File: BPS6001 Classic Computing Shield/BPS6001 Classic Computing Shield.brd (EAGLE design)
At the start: 119.4 x 58.7 mm, 85 parts, among them IC1 MAX3232CSE, X1 VGA

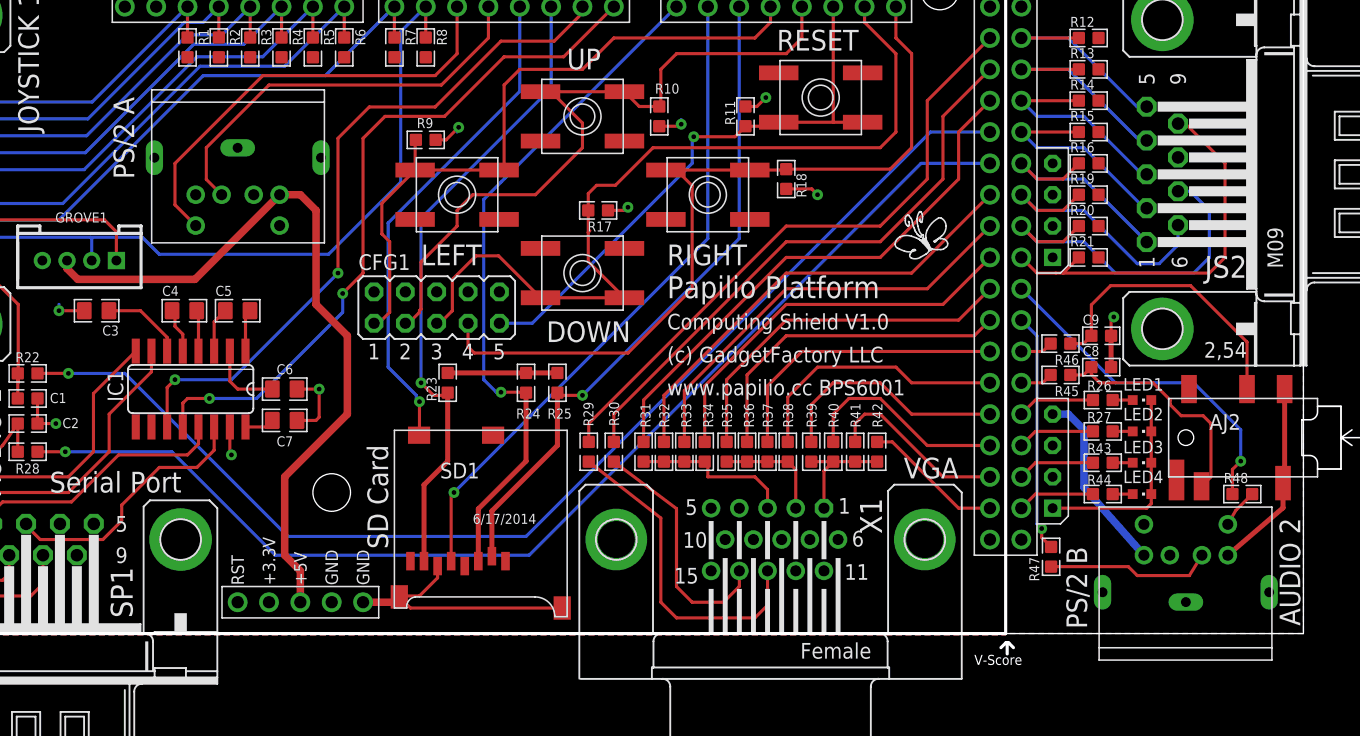
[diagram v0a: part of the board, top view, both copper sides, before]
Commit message: Fix the PS/2 connectors.
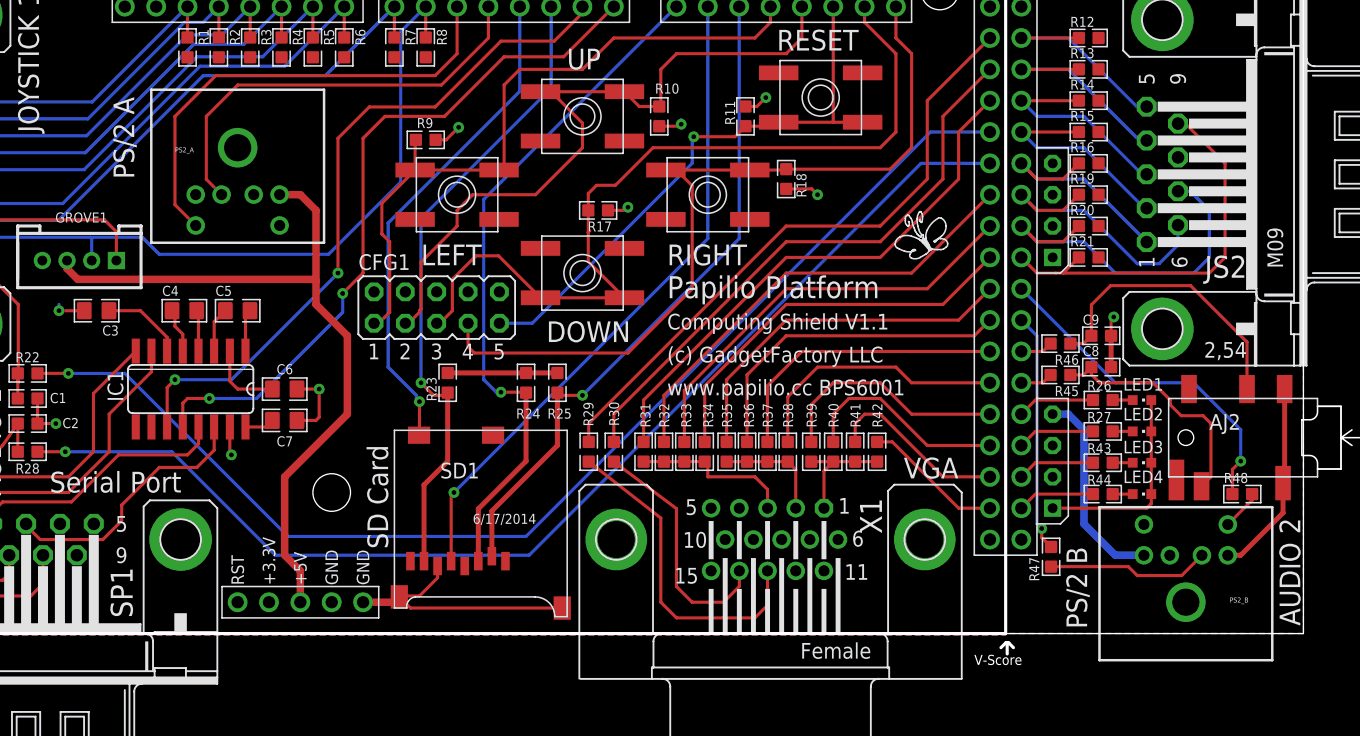
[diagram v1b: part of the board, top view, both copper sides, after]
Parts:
- PS2_A, PS2_B: value CON_PS/2 -> MINI-DIN6PTH; device usb1:PS/2 -> SparkFun-Connectors:MINI-DIN6
- moved PS2_A 8.51 mm to (33.0, 44.1)
- moved PS2_B 8.51 mm to (109.9, -2.16)
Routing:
- net PS2CLK1: track 36.1 -> 38.3 mm
- net 5V0_PS2: track 15.1 -> 16.6 mm
- net PS2DAT1: track 33.4 -> 34.9 mm
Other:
- board text added: "Computing Shield V1.1"
- board text removed: "Computing Shield V1.0"
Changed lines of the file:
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@@
 <setting verticaltext="up"/>
 </settings>
-<grid distance="0.05" unitdist="inch" unit="mm" style="lines" multiple="1" display="yes" altdistance="0.005" altunitdist="inch" altunit="inch"/>
+<grid distance="0.05" unitdist="inch" unit="inch" style="lines" multiple="1" display="yes" altdistance="0.005" altunitdist="inch" altunit="inch"/>
 <layers>
 <layer number="1" name="Top" color="4" fill="1" visible="yes" active="yes"/>
@@
 <wire x1="0" y1="0" x2="0" y2="55.88" width="0.254" layer="20"/>
 <text x="67.818" y="27.178" size="1.778" layer="21" ratio="12">Papilio Platform</text>
-<text x="67.818" y="24.638" size="1.27" layer="21" ratio="10">Computing Shield V1.0</text>
+<text x="67.818" y="24.638" size="1.27" layer="21" ratio="10">Computing Shield V1.1</text>
 <text x="24.638" y="36.83" size="1.6764" layer="21" ratio="15" rot="R90">PS/2 A</text>
 <text x="103.759" y="53.34" size="1.6764" layer="21" ratio="15">Joystick 2</text>
@@
 <attribute name="BOM" value="EXCLUDE" x="88.519" y="31.75" size="1.778" layer="27" display="off"/>
 </element>
-<element name="PS2_B" library="usb1" package="PS/2" value="CON_PS/2" x="109.855" y="6.35" rot="R180">
-<attribute name="PARTNO" value="MD-60S" x="109.855" y="6.35" size="1.778" layer="27" rot="R180" display="off"/>
-</element>
-<element name="PS2_A" library="usb1" package="PS/2" value="CON_PS/2" x="33.02" y="35.56">
-<attribute name="PARTNO" value="MD-60S" x="33.02" y="35.56" size="1.778" layer="27" display="off"/>
-</element>
 <element name="R9" library="GadgetFactory" package="0603" value="47K" x="48.26" y="40.005" smashed="yes" rot="R180">
 <attribute name="NAME" x="48.871" y="41.772" size="0.8128" layer="25" font="vector" ratio="16" rot="R180"/>
@@
 <attribute name="PARTNO" value="M20-9720545" x="49.149" y="26.416" size="1.778" layer="27" display="off"/>
 </element>
+<element name="PS2_B" library="SparkFun-Connectors" package="MINI-DIN6" value="MINI-DIN6PTH" x="109.855" y="-2.159" rot="R180"/>
+<element name="PS2_A" library="SparkFun-Connectors" package="MINI-DIN6" value="MINI-DIN6PTH" x="33.02" y="44.069"/>
 </elements>
 <signals>
@@
 <contactref element="R18" pad="1"/>
 <contactref element="R11" pad="1"/>
-<contactref element="PS2_A" pad="3"/>
 <polygon width="0.254" layer="16">
 <vertex x="0" y="-0.127"/>
@@
 <wire x1="64.643" y1="34.544" x2="64.643" y2="34.798" width="0.254" layer="16"/>
 <contactref element="GROVE1" pad="4"/>
+<contactref element="PS2_A" pad="3"/>
+<contactref element="PS2_A" pad="3"/>
 </signal>
 <signal name="HORIZONTAL_SYNC">
@@
 </signal>
 <signal name="PS2CLK1">
-<contactref element="PS2_A" pad="5"/>
 <contactref element="H1" pad="D5"/>
 <wire x1="50.8" y1="50.8" x2="50.8" y2="46.99" width="0.254" layer="1"/>
 <wire x1="50.8" y1="46.99" x2="49.022" y2="45.212" width="0.254" layer="1"/>
-<wire x1="49.022" y1="45.212" x2="35.052" y2="45.212" width="0.254" layer="1"/>
-<wire x1="35.052" y1="45.212" x2="27.94" y2="38.1" width="0.254" layer="1"/>
-<wire x1="27.94" y1="38.1" x2="27.94" y2="34.74" width="0.254" layer="1"/>
-<wire x1="27.94" y1="34.74" x2="29.62" y2="33.06" width="0.254" layer="1"/>
+<wire x1="49.022" y1="45.212" x2="31.242" y2="45.212" width="0.254" layer="1"/>
+<contactref element="PS2_A" pad="5"/>
+<wire x1="31.242" y1="45.212" x2="27.94" y2="41.91" width="0.254" layer="1"/>
+<wire x1="27.94" y1="41.91" x2="27.94" y2="34.749" width="0.254" layer="1"/>
+<wire x1="27.94" y1="34.749" x2="29.62" y2="33.069" width="0.254" layer="1"/>
 </signal>
 <signal name="RED1">
@@
 </signal>
 <signal name="5V0">
-<contactref element="PS2_A" pad="4"/>
 <contactref element="H1" pad="5V@0"/>
 <wire x1="41.91" y1="24.13" x2="39.37" y2="26.67" width="0.6096" layer="1"/>
-<wire x1="39.37" y1="26.67" x2="39.37" y2="34.29" width="0.6096" layer="1"/>
+<wire x1="39.37" y1="26.67" x2="39.37" y2="28.575" width="0.6096" layer="1"/>
+<wire x1="39.37" y1="28.575" x2="39.37" y2="34.29" width="0.6096" layer="1"/>
 <wire x1="39.37" y1="34.29" x2="38.1" y2="35.56" width="0.6096" layer="1"/>
-<wire x1="38.1" y1="35.56" x2="36.42" y2="35.56" width="0.6096" layer="1"/>
 <wire x1="41.91" y1="24.13" x2="41.91" y2="17.78" width="0.6096" layer="1"/>
 <wire x1="41.91" y1="17.78" x2="36.83" y2="12.7" width="0.6096" layer="1"/>
@@
 <wire x1="19.193" y1="30.226" x2="19.193" y2="29.575" width="0.6096" layer="1"/>
 <wire x1="19.193" y1="29.575" x2="20.066" y2="28.702" width="0.6096" layer="1"/>
-<wire x1="20.066" y1="28.702" x2="29.562" y2="28.702" width="0.6096" layer="1"/>
-<wire x1="29.562" y1="28.702" x2="36.42" y2="35.56" width="0.6096" layer="1"/>
+<contactref element="PS2_A" pad="4"/>
+<contactref element="PS2_A" pad="4"/>
+<wire x1="38.1" y1="35.56" x2="36.429" y2="35.56" width="0.6096" layer="1"/>
+<wire x1="36.429" y1="35.56" x2="36.42" y2="35.569" width="0.6096" layer="1"/>
+<wire x1="20.066" y1="28.702" x2="39.243" y2="28.702" width="0.6096" layer="1"/>
+<wire x1="39.243" y1="28.702" x2="39.37" y2="28.575" width="0.6096" layer="1"/>
 </signal>
 <signal name="PS2DAT2">
@@
 </signal>
 <signal name="PS2DAT1">
-<contactref element="PS2_A" pad="1"/>
 <contactref element="H1" pad="D4"/>
 <wire x1="53.34" y1="50.8" x2="53.34" y2="48.26" width="0.254" layer="1"/>
 <wire x1="53.34" y1="48.26" x2="49.53" y2="44.45" width="0.254" layer="1"/>
-<wire x1="49.53" y1="44.45" x2="35.56" y2="44.45" width="0.254" layer="1"/>
-<wire x1="35.56" y1="44.45" x2="30.48" y2="39.37" width="0.254" layer="1"/>
-<wire x1="30.48" y1="39.37" x2="30.48" y2="36.8" width="0.254" layer="1"/>
-<wire x1="30.48" y1="36.8" x2="31.72" y2="35.56" width="0.254" layer="1"/>
+<wire x1="49.53" y1="44.45" x2="33.02" y2="44.45" width="0.254" layer="1"/>
+<contactref element="PS2_A" pad="1"/>
+<wire x1="33.02" y1="44.45" x2="30.48" y2="41.91" width="0.254" layer="1"/>
+<wire x1="30.48" y1="41.91" x2="30.48" y2="36.809" width="0.254" layer="1"/>
+<wire x1="30.48" y1="36.809" x2="31.72" y2="35.569" width="0.254" layer="1"/>
 </signal>
 <signal name="SD_SCK">
@@
 <contactref element="LED2" pad="C"/>
 <contactref element="LED1" pad="C"/>
-<contactref element="PS2_B" pad="3"/>
 <contactref element="PWR_2" pad="P1"/>
 <contactref element="PWR_1" pad="P1"/>
@@
 <wire x1="117.856" y1="19.812" x2="117.856" y2="12.319" width="0.4064" layer="1"/>
 <wire x1="117.856" y1="12.319" x2="117.729" y2="12.192" width="0.4064" layer="1"/>
-<wire x1="117.729" y1="12.192" x2="117.729" y2="10.189" width="0.4064" layer="1"/>
-<wire x1="117.729" y1="10.189" x2="113.255" y2="6.35" width="0.4064" layer="1"/>
+<wire x1="117.729" y1="12.192" x2="117.729" y2="9.779" width="0.4064" layer="1"/>
+<contactref element="PS2_B" pad="3"/>
+<wire x1="117.729" y1="9.779" x2="114.3" y2="6.35" width="0.4064" layer="1"/>
+<wire x1="114.3" y1="6.35" x2="113.264" y2="6.35" width="0.4064" layer="1"/>
+<wire x1="113.264" y1="6.35" x2="113.255" y2="6.341" width="0.4064" layer="1"/>
 </signal>
 <signal name="AUDIO1-LEFT">
@@
 </signal>
 <signal name="5V0_PS2">
-<contactref element="PS2_B" pad="4"/>
 <wire x1="100.33" y1="17.78" x2="101.6" y2="16.51" width="0.6096" layer="16"/>
-<wire x1="101.6" y1="16.51" x2="101.6" y2="11.84" width="0.6096" layer="16"/>
-<wire x1="101.6" y1="11.84" x2="106.455" y2="6.35" width="0.6096" layer="16"/>
+<wire x1="101.6" y1="16.51" x2="101.6" y2="8.89" width="0.6096" layer="16"/>
 <contactref element="PWR_2" pad="P4"/>
 <wire x1="100.33" y1="17.78" x2="99.06" y2="17.78" width="0.6096" layer="16"/>
+<contactref element="PS2_B" pad="4"/>
+<wire x1="101.6" y1="8.89" x2="104.14" y2="6.35" width="0.6096" layer="16"/>
+<wire x1="104.14" y1="6.35" x2="106.446" y2="6.35" width="0.6096" layer="16"/>
+<wire x1="106.446" y1="6.35" x2="106.455" y2="6.341" width="0.6096" layer="16"/>
 </signal>
 <signal name="SW_RIGHT">
@@
 </signal>
 <signal name="N$16">
-<contactref element="PS2_B" pad="1"/>
 <contactref element="R47" pad="2"/>
 <wire x1="98.933" y1="5.423" x2="105.194" y2="5.423" width="0.254" layer="1"/>
 <wire x1="105.194" y1="5.423" x2="105.918" y2="4.699" width="0.254" layer="1"/>
-<wire x1="105.918" y1="4.699" x2="110.139" y2="4.699" width="0.254" layer="1"/>
-<wire x1="110.139" y1="4.699" x2="111.155" y2="6.35" width="0.254" layer="1"/>
+<contactref element="PS2_B" pad="1"/>
+<wire x1="105.918" y1="4.699" x2="109.513" y2="4.699" width="0.254" layer="1"/>
+<wire x1="109.513" y1="4.699" x2="111.155" y2="6.341" width="0.254" layer="1"/>
 </signal>
 <signal name="N$17">
+<contactref element="R48" pad="2"/>
 <contactref element="PS2_B" pad="5"/>
-<contactref element="R48" pad="2"/>
-<wire x1="113.255" y1="8.85" x2="113.89" y2="9.966" width="0.254" layer="1"/>
-<wire x1="113.89" y1="9.966" x2="115.227" y2="11.303" width="0.254" layer="1"/>
+<wire x1="115.227" y1="11.303" x2="115.227" y2="10.813" width="0.254" layer="1"/>
+<wire x1="115.227" y1="10.813" x2="113.255" y2="8.841" width="0.254" layer="1"/>
 </signal>
 </signals>

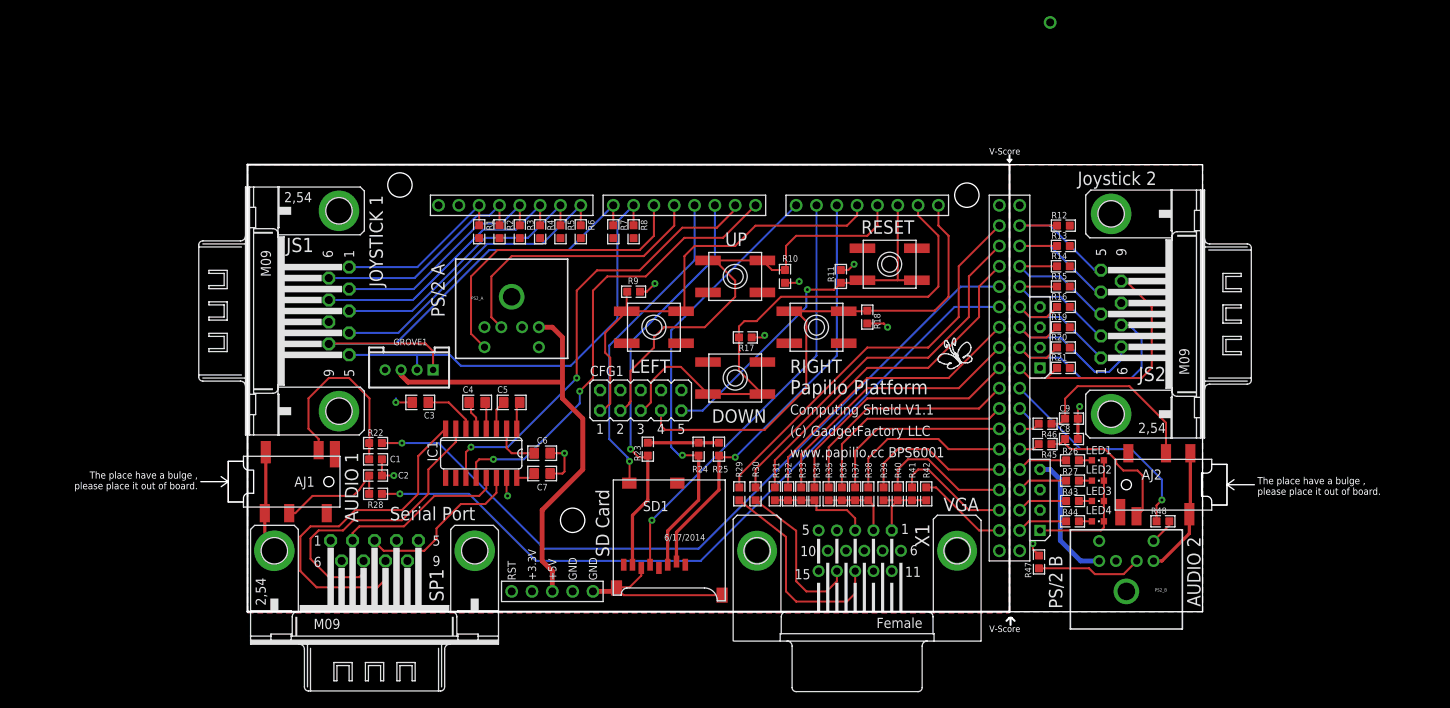
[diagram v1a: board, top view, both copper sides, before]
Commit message: Rotated the Classic Computing Shield 180 degrees to make it more accessible.
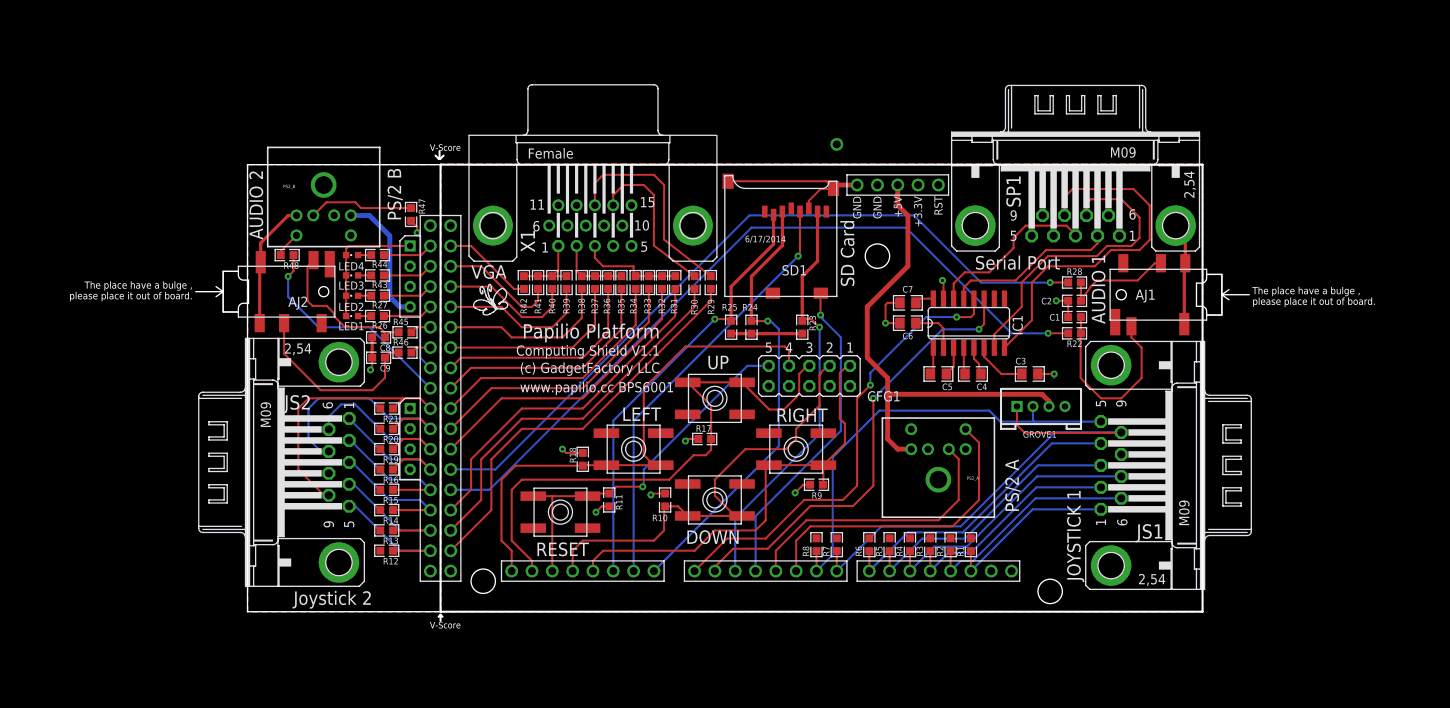
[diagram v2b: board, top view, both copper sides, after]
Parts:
- moved H1 131.8 mm to (119.4, 55.9), turned to 180 degrees
- moved PS2_B 117.0 mm to (9.53, 58.0), turned to 0 degrees
- moved R48 114.4 mm to (4.95, 44.6), turned to 180 degrees
- moved AJ2 114.1 mm to (3.94, 40.0), turned to 180 degrees
- moved AJ1 112.7 mm to (114.8, 39.6), turned to 0 degrees
- moved LED4 99.0 mm to (13.1, 44.6), turned to 90 degrees
- moved JS1 98.4 mm to (108.0, 18.3), turned to 90 degrees
- moved JS2 98.3 mm to (11.4, 18.7), turned to 270 degrees
- moved LED3 97.4 mm to (13.1, 42.0), turned to 90 degrees
- moved SP1 96.6 mm to (103.5, 48.3), turned to 180 degrees
- moved LED2 96.0 mm to (13.1, 39.5), turned to 90 degrees
- moved U$2 95.8 mm to (100.3, 2.54), turned to 180 degrees
- moved LED1 94.9 mm to (13.1, 37.0), turned to 90 degrees
- moved R12 93.8 mm to (17.4, 7.62), turned to 180 degrees
- moved R44 93.0 mm to (16.3, 44.6), turned to 0 degrees
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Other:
- outline, holes or cut-outs redrawn
